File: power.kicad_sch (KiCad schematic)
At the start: 12 parts, among them J1 Conn_01x06_Pin, U3 LM66100DCK, U4 TPS62A01DRLR, U5 TPS22918TDBVRQ1

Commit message: Update power.kicad_sch
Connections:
- net +5V: no longer J1.3 (Pin_3)
- net GND: no longer J1.4 (Pin_4)
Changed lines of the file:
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@@
 	(wire
 		(pts
-			(xy 24.13 92.71) (xy 40.64 92.71)
+			(xy 24.13 92.71) (xy 36.83 92.71)
 		)
 		(stroke
@@
 	(wire
 		(pts
-			(xy 24.13 95.25) (xy 36.83 95.25)
+			(xy 148.59 64.77) (xy 160.02 64.77)
 		)
 		(stroke
@@
 	(wire
 		(pts
-			(xy 148.59 64.77) (xy 160.02 64.77)
+			(xy 148.59 74.93) (xy 160.02 74.93)
 		)
 		(stroke
@@
 	(wire
 		(pts
-			(xy 148.59 74.93) (xy 160.02 74.93)
+			(xy 172.72 72.39) (xy 176.53 72.39)
 		)
 		(stroke
@@
 	(wire
 		(pts
-			(xy 172.72 72.39) (xy 176.53 72.39)
+			(xy 172.72 64.77) (xy 180.34 64.77)
 		)
 		(stroke
@@
 	(wire
 		(pts
-			(xy 172.72 64.77) (xy 180.34 64.77)
+			(xy 160.02 64.77) (xy 172.72 64.77)
 		)
 		(stroke
@@
 	(wire
 		(pts
-			(xy 160.02 64.77) (xy 172.72 64.77)
+			(xy 160.02 64.77) (xy 160.02 66.04)
 		)
 		(stroke
@@
 	(wire
 		(pts
-			(xy 24.13 97.79) (xy 40.64 97.79)
+			(xy 44.45 69.85) (xy 44.45 82.55)
 		)
 		(stroke
@@
 	(wire
 		(pts
-			(xy 160.02 64.77) (xy 160.02 66.04)
+			(xy 67.31 82.55) (xy 67.31 64.77)
 		)
 		(stroke
@@
 	(wire
 		(pts
-			(xy 44.45 69.85) (xy 44.45 82.55)
-		)
-		(stroke
-			(width 0)
-			(type default)
-		)
-	)
-	(wire
-		(pts
-			(xy 67.31 82.55) (xy 67.31 64.77)
-		)
-		(stroke
-			(width 0)
-			(type default)
-		)
-	)
-	(wire
-		(pts
 			(xy 44.45 82.55) (xy 67.31 82.55)
-		)
-		(stroke
-			(width 0)
-			(type default)
-		)
-	)
-	(wire
-		(pts
-			(xy 36.83 102.87) (xy 40.64 102.87)
 		)
 		(stroke
@@
 	)
 	(symbol
-		(lib_id "power:GND")
-		(at 40.64 97.79 90)
-		(unit 1)
-		(exclude_from_sim no)
-		(in_bom yes)
-		(on_board yes)
-		(dnp no)
-		(fields_autoplaced yes)
-		(property "Reference" "#PWR033"
-			(at 46.99 97.79 0)
-			(effects
-				(font
-					(size 1.27 1.27)
-				)
-				(hide yes)
-			)
-		)
-		(property "Value" "GND"
-			(at 44.45 97.7899 90)
-			(effects
-				(font
-					(size 1.27 1.27)
-				)
-				(justify right)
-			)
-		)
-		(property "Footprint" ""
-			(at 40.64 97.79 0)
-			(effects
-				(font
-					(size 1.27 1.27)
-				)
-				(hide yes)
-			)
-		)
-		(property "Datasheet" ""
-			(at 40.64 97.79 0)
-			(effects
-				(font
-					(size 1.27 1.27)
-				)
-				(hide yes)
-			)
-		)
-		(property "Description" "Power symbol creates a global label with name \"GND\" , ground"
-			(at 40.64 97.79 0)
-			(effects
-				(font
-					(size 1.27 1.27)
-				)
-				(hide yes)
-			)
-		)
-		(pin "1"
-		)
-		(instances
-			(project ""
-				(path "/45f99759-2553-47c9-8640-9aec1810c6cc/7b2d3bba-bbf7-4c7f-a096-b989c0e14168"
-					(reference "#PWR033")
-					(unit 1)
-				)
-			)
-		)
-	)
-	(symbol
 		(lib_id "Device:C")
 		(at 172.72 68.58 0)
@@
 	)
 	(symbol
-		(lib_id "power:+5V")
-		(at 36.83 95.25 270)
-		(unit 1)
-		(exclude_from_sim no)
-		(in_bom yes)
-		(on_board yes)
-		(dnp no)
-		(fields_autoplaced yes)
-		(property "Reference" "#PWR045"
-			(at 33.02 95.25 0)
-			(effects
-				(font
-					(size 1.27 1.27)
-				)
-				(hide yes)
-			)
-		)
-		(property "Value" "+5V"
-			(at 40.64 95.2499 90)
-			(effects
-				(font
-					(size 1.27 1.27)
-				)
-				(justify left)
-			)
-		)
-		(property "Footprint" ""
-			(at 36.83 95.25 0)
-			(effects
-				(font
-					(size 1.27 1.27)
-				)
-				(hide yes)
-			)
-		)
-		(property "Datasheet" ""
-			(at 36.83 95.25 0)
-			(effects
-				(font
-					(size 1.27 1.27)
-				)
-				(hide yes)
-			)
-		)
-		(property "Description" "Power symbol creates a global label with name \"+5V\""
-			(at 36.83 95.25 0)
-			(effects
-				(font
-					(size 1.27 1.27)
-				)
-				(hide yes)
-			)
-		)
-		(pin "1"
-		)
-		(instances
-			(project ""
-				(path "/45f99759-2553-47c9-8640-9aec1810c6cc/7b2d3bba-bbf7-4c7f-a096-b989c0e14168"
-					(reference "#PWR045")
-					(unit 1)
-				)
-			)
-		)
-	)
-	(symbol
 		(lib_id "Device:C")
 		(at 107.95 83.82 0)
@@
 	(symbol
 		(lib_id "power:GND")
-		(at 40.64 92.71 90)
+		(at 36.83 92.71 90)
 		(unit 1)
 		(exclude_from_sim no)
@@
 		(fields_autoplaced yes)
 		(property "Reference" "#PWR032"
-			(at 46.99 92.71 0)
+			(at 43.18 92.71 0)
 			(effects
 				(font
@@
 		)
 		(property "Value" "GND"
-			(at 44.45 92.7099 90)
+			(at 40.64 92.7099 90)
 			(effects
 				(font
@@
 		)
 		(property "Footprint" ""
-			(at 40.64 92.71 0)
+			(at 36.83 92.71 0)
 			(effects
 				(font
@@
 		)
 		(property "Datasheet" ""
-			(at 40.64 92.71 0)
+			(at 36.83 92.71 0)
 			(effects
 				(font
@@
 		)
 		(property "Description" "Power symbol creates a global label with name \"GND\" , ground"
-			(at 40.64 92.71 0)
+			(at 36.83 92.71 0)
 			(effects
 				(font
@@
 	(symbol
 		(lib_id "power:GND")
-		(at 40.64 102.87 90)
+		(at 36.83 102.87 90)
 		(unit 1)
 		(exclude_from_sim no)
@@
 		(fields_autoplaced yes)
 		(property "Reference" "#PWR034"
-			(at 46.99 102.87 0)
+			(at 43.18 102.87 0)
 			(effects
 				(font
@@
 		)
 		(property "Value" "GND"
-			(at 44.45 102.8699 90)
+			(at 40.64 102.8699 90)
 			(effects
 				(font
@@
 		)
 		(property "Footprint" ""
-			(at 40.64 102.87 0)
+			(at 36.83 102.87 0)
 			(effects
 				(font
@@
 		)
 		(property "Datasheet" ""
-			(at 40.64 102.87 0)
+			(at 36.83 102.87 0)
 			(effects
 				(font
@@
 		)
 		(property "Description" "Power symbol creates a global label with name \"GND\" , ground"
-			(at 40.64 102.87 0)
-			(effects
-				(font
+			(at 36.83 102.87 0)
+			(effects
+				(font

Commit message: Ripple Filter
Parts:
- removed U4: TPS62A01DRLR, SOT6_DRL_TEX, symbol TPS62A01:TPS62A01DRLR
- added C11: 10uF, symbol Device:C
- added C12: 22uF, symbol Device:C
- added L5: 10uH, symbol Device:L
- added R11: 1, symbol Device:R_US
- C6: value 1nF -> 330pF
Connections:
- net 5V_SW: now also L5.1
- net GND: now also C11.1, C12.2
- new net: C12.1, R11.2
- new net 5V_F: C11.2, L5.2, R11.1
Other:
- added sheet D_Filter_Sim (untitled.kicad_sch)
- moved on the sheet: C6

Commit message: Ripple Filter
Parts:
- removed C4: 100n, symbol Device:C
- added R12: 100k, symbol Device:R_US
- R7: value 1k -> 10k
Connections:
- net GND: now also R12.2; no longer R7.2
- net RF_PWR_EN: now also R7.1; no longer U5.3 (ON)
- net at C5.1, U3.3 (~{CE}), U3.6 (VOUT)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: no longer R7.1
- new net: R12.1, R7.2, U5.3 (ON)
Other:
- removed sheet D_Filter_Sim
- note added: "LC low-pass for PWR-2/4 ripple"
- moved on the sheet: C5, R8

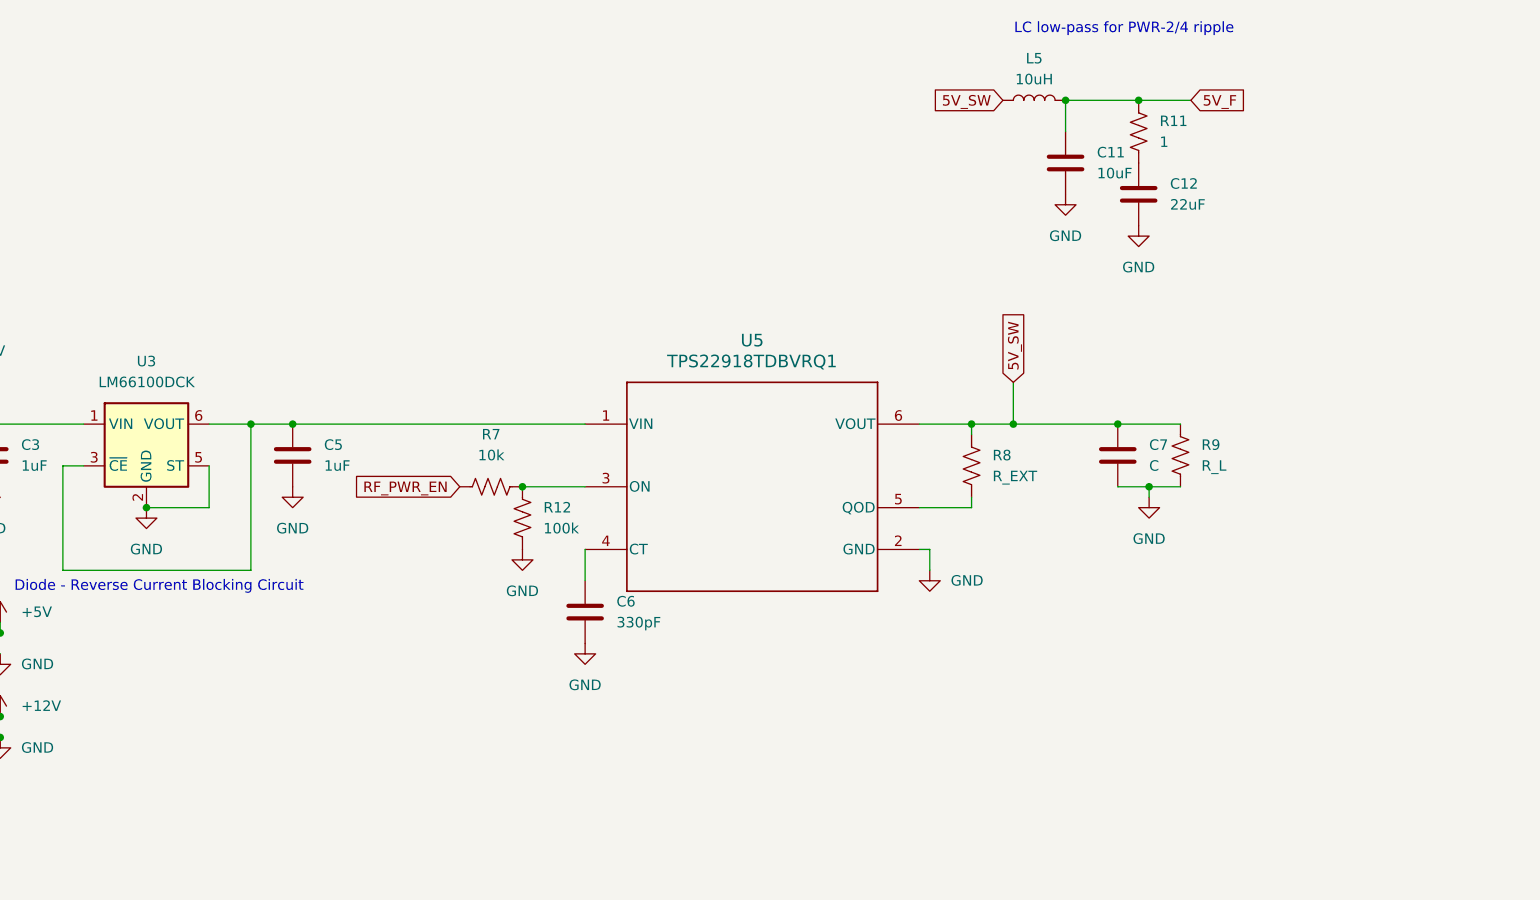
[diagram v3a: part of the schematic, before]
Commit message: Placing both LDOs
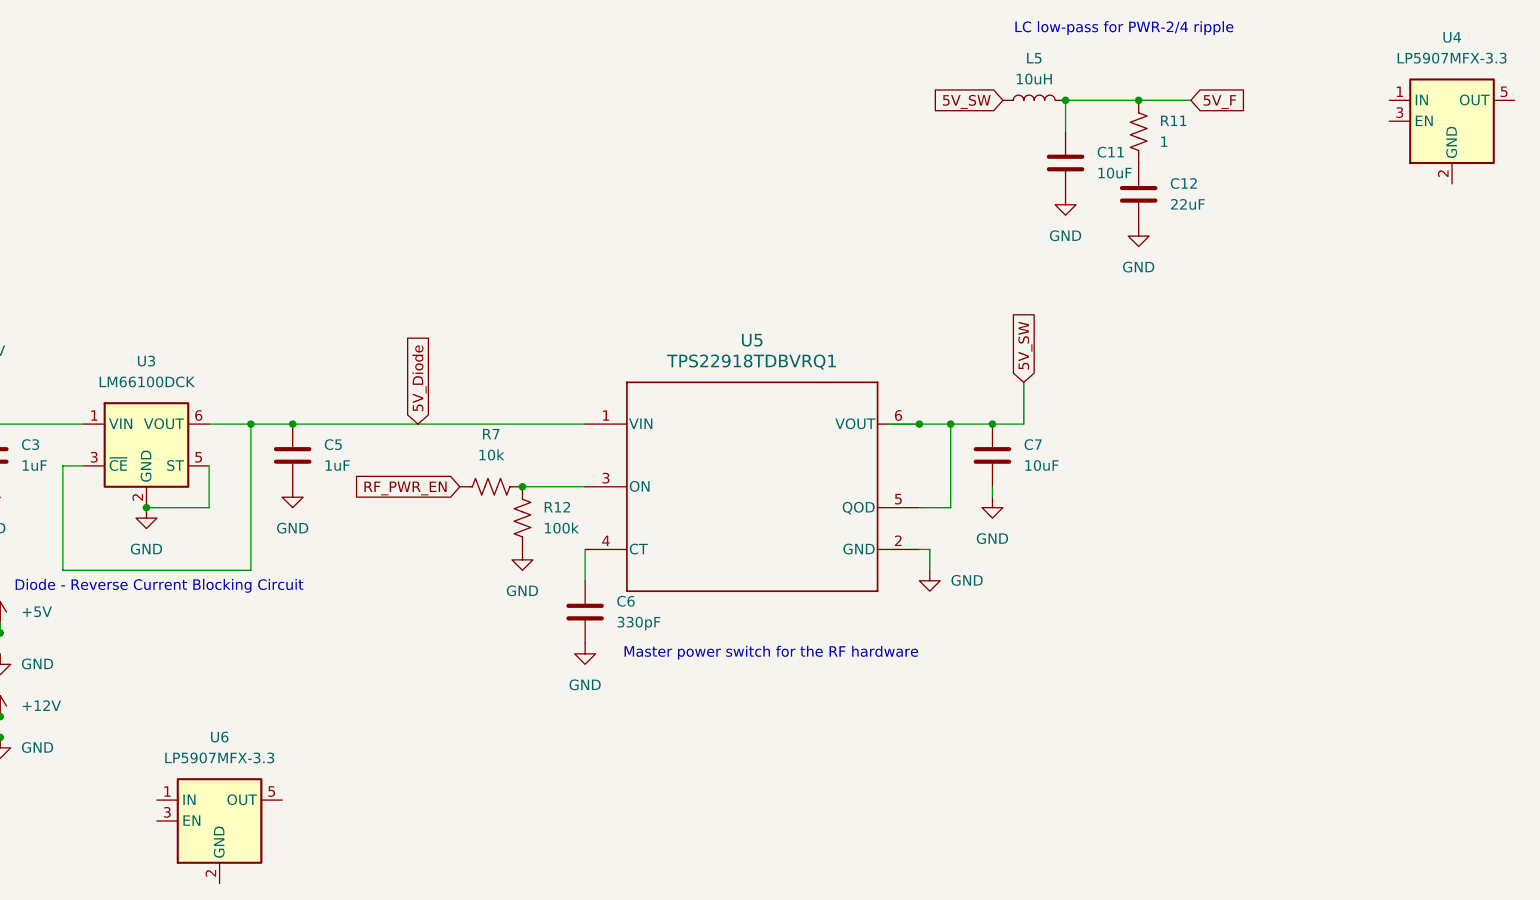
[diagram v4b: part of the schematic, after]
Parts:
- removed R8: R_EXT, symbol Device:R_US
- removed R9: R_L, symbol Device:R_US
- added U4, U6: LP5907MFX-3.3, Package_TO_SOT_SMD:SOT-23-5, symbol Regulator_Linear:LP5907MFX-3.3
- C7: value C -> 10uF
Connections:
- net 5V_SW: now also U5.5 (QOD)
- net 5V_Diode: now reaches C5.1, U3.3 (~{CE}), U3.6 (VOUT), U5.1 (VIN)
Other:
- note added: "Master power switch for the RF hardware"
- moved on the sheet: C7

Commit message: LDO
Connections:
- net 5V_F: now also U4.1 (IN)
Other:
- moved on the sheet: U4
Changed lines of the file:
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@@
+		)
+	)
+	(global_label "5V_F"
+		(shape input)
+		(at 213.36 41.91 180)
+		(fields_autoplaced yes)
+		(effects
+			(font
+				(size 1.27 1.27)
+			)
+			(justify right)
+		)
+		(property "Intersheetrefs" "${INTERSHEET_REFS}"
+			(at 206.0205 41.91 0)
+			(effects
+				(font
+					(size 1.27 1.27)
+				)
+				(justify right)
+				(hide yes)
+			)
 		)
 	)
@@
 	(symbol
 		(lib_id "Regulator_Linear:LP5907MFX-3.3")
-		(at 213.36 27.94 0)
+		(at 220.98 44.45 0)
 		(unit 1)
 		(exclude_from_sim no)
@@
 		(fields_autoplaced yes)
 		(property "Reference" "U4"
-			(at 213.36 17.78 0)
+			(at 220.98 34.29 0)
 			(effects
 				(font
@@
 		)
 		(property "Value" "LP5907MFX-3.3"
-			(at 213.36 20.32 0)
+			(at 220.98 36.83 0)
 			(effects
 				(font
@@
 		)
 		(property "Footprint" "Package_TO_SOT_SMD:SOT-23-5"
-			(at 213.36 19.05 0)
+			(at 220.98 35.56 0)
 			(effects
 				(font
@@
 		)
 		(property "Datasheet" "http://www.ti.com/lit/ds/symlink/lp5907.pdf"
-			(at 213.36 15.24 0)
+			(at 220.98 31.75 0)
 			(effects
 				(font
@@
 		)
 		(property "Description" "250-mA Ultra-Low-Noise Low-IQ LDO, 3.3V, SOT-23"
-			(at 213.36 27.94 0)
-			(effects
-				(font
+			(at 220.98 44.45 0)
+			(effects
+				(font

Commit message: LDOs
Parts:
- removed U4, U6: LP5907MFX-3.3, Package_TO_SOT_SMD:SOT-23-5, symbol Regulator_Linear:LP5907MFX-3.3
- added U13, U4, U6: LP5907MFX-3.0, Package_TO_SOT_SMD:SOT-23-5, symbol Regulator_Linear:LP5907MFX-3.0
- added U14: LP5907MFX-4.5, Package_TO_SOT_SMD:SOT-23-5, symbol Regulator_Linear:LP5907MFX-4.5
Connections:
- net 5V_F: now also U13.1 (IN)
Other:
- note added: "LDO for RF"
- note added: "LDO for Telemetry"
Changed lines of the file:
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@@
+	)
+	(junction
+		(at 87.63 64.77)
+		(diameter 0)
+		(color 0 0 0 0)
 	)
 	(junction
@@
 	(wire
 		(pts
+			(xy 87.63 62.23) (xy 87.63 64.77)
+		)
+		(stroke
+			(width 0)
+			(type default)
+		)
+	)
+	(wire
+		(pts
 			(xy 166.37 25.4) (xy 175.26 25.4)
 		)
@@
 	(wire
 		(pts
+			(xy 87.63 64.77) (xy 107.95 64.77)
+		)
+		(stroke
+			(width 0)
+			(type default)
+		)
+	)
+	(wire
+		(pts
 			(xy 62.23 69.85) (xy 62.23 74.93)
 		)
@@
 	(wire
 		(pts
-			(xy 72.39 64.77) (xy 107.95 64.77)
+			(xy 72.39 64.77) (xy 87.63 64.77)
 		)
 		(stroke
@@
 		)
 	)
+	(text "LDO for Telemetry"
+		(exclude_from_sim no)
+		(at 62.484 118.11 0)
+		(effects
+			(font
+				(size 1.27 1.27)
+			)
+		)
+	)
 	(text "Master power switch for the RF hardware"
 		(exclude_from_sim no)
@@
 		)
 	)
+	(text "LDO for RF"
+		(exclude_from_sim no)
+		(at 221.234 55.372 0)
+		(effects
+			(font
+				(size 1.27 1.27)
+			)
+		)
+	)
 	(global_label "5V_F"
 		(shape input)
@@
 	(global_label "5V_Diode"
 		(shape input)
-		(at 87.63 64.77 90)
+		(at 87.63 62.23 90)
 		(fields_autoplaced yes)
 		(effects
@@
 		)
 		(property "Intersheetrefs" "${INTERSHEET_REFS}"
-			(at 87.63 53.2577 90)
+			(at 87.63 50.7177 90)
 			(effects
 				(font
@@
 	)
 	(symbol
+		(lib_id "Regulator_Linear:LP5907MFX-3.0")
+		(at 38.1 149.86 0)
+		(unit 1)
+		(exclude_from_sim no)
+		(in_bom yes)
+		(on_board yes)
+		(dnp no)
+		(fields_autoplaced yes)
+		(property "Reference" "U6"
+			(at 38.1 139.7 0)
+			(effects
+				(font
+					(size 1.27 1.27)
+				)
+			)
+		)
+		(property "Value" "LP5907MFX-3.0"
+			(at 38.1 142.24 0)
+			(effects
+				(font
+					(size 1.27 1.27)
+				)
+			)
+		)
+		(property "Footprint" "Package_TO_SOT_SMD:SOT-23-5"
+			(at 38.1 140.97 0)
+			(effects
+				(font
+					(size 1.27 1.27)
+				)
+				(hide yes)
+			)
+		)
+		(property "Datasheet" "http://www.ti.com/lit/ds/symlink/lp5907.pdf"
+			(at 38.1 137.16 0)
+			(effects
+				(font
+					(size 1.27 1.27)
+				)
+				(hide yes)
+			)
+		)
+		(property "Description" "250-mA Ultra-Low-Noise Low-IQ LDO, 3.0V, SOT-23"
+			(at 38.1 149.86 0)
+			(effects
+				(font
+					(size 1.27 1.27)
+				)
+				(hide yes)
+			)
+		)
+		(pin "3"
+		)
+		(pin "1"
+		)
+		(pin "2"
+		)
+		(pin "4"
+		)
+		(pin "5"
+		)
+		(instances
+			(project "VIP_direct_sampling_board"
+				(path "/45f99759-2553-47c9-8640-9aec1810c6cc/7b2d3bba-bbf7-4c7f-a096-b989c0e14168"
+					(reference "U6")
+					(unit 1)
+				)
+			)
+		)
+	)
+	(symbol
+		(lib_id "Regulator_Linear:LP5907MFX-3.0")
+		(at 220.98 44.45 0)
+		(unit 1)
+		(exclude_from_sim no)
+		(in_bom yes)
+		(on_board yes)
+		(dnp no)
+		(fields_autoplaced yes)
+		(property "Reference" "U13"
+			(at 220.98 34.29 0)
+			(effects
+				(font
+					(size 1.27 1.27)
+				)
+			)
+		)
+		(property "Value" "LP5907MFX-3.0"
+			(at 220.98 36.83 0)
+			(effects
+				(font
+					(size 1.27 1.27)
+				)
+			)
+		)
+		(property "Footprint" "Package_TO_SOT_SMD:SOT-23-5"
+			(at 220.98 35.56 0)
+			(effects
+				(font
+					(size 1.27 1.27)
+				)
+				(hide yes)
+			)
+		)
+		(property "Datasheet" "http://www.ti.com/lit/ds/symlink/lp5907.pdf"
+			(at 220.98 31.75 0)
+			(effects
+				(font
+					(size 1.27 1.27)
+				)
+				(hide yes)
+			)
+		)
+		(property "Description" "250-mA Ultra-Low-Noise Low-IQ LDO, 3.0V, SOT-23"
+			(at 220.98 44.45 0)
+			(effects
+				(font
+					(size 1.27 1.27)
+				)
+				(hide yes)
+			)
+		)
+		(pin "3"
+		)
+		(pin "1"
+		)
+		(pin "2"
+		)
+		(pin "4"
+		)
+		(pin "5"
+		)
+		(instances
+			(project ""
+				(path "/45f99759-2553-47c9-8640-9aec1810c6cc/7b2d3bba-bbf7-4c7f-a096-b989c0e14168"
+					(reference "U13")
+					(unit 1)
+				)
+			)
+		)
+	)
+	(symbol
 		(lib_id "Device:C")
 		(at 157.48 68.58 0)
@@
 	)
 	(symbol
-		(lib_id "Regulator_Linear:LP5907MFX-3.3")
-		(at 63.5 113.03 0)
-		(unit 1)
-		(exclude_from_sim no)
-		(in_bom yes)
-		(on_board yes)
-		(dnp no)
-		(fields_autoplaced yes)
-		(property "Reference" "U6"
-			(at 63.5 102.87 0)
-			(effects
-				(font
-					(size 1.27 1.27)
-				)
-			)
-		)
-		(property "Value" "LP5907MFX-3.3"
-			(at 63.5 105.41 0)
+		(lib_id "Regulator_Linear:LP5907MFX-4.5")
+		(at 101.6 151.13 0)
+		(unit 1)
+		(exclude_from_sim no)
+		(in_bom yes)
+		(on_board yes)
+		(dnp no)
+		(fields_autoplaced yes)
+		(property "Reference" "U14"
+			(at 101.6 140.97 0)
+			(effects
+				(font
+					(size 1.27 1.27)
+				)
+			)
+		)
+		(property "Value" "LP5907MFX-4.5"
+			(at 101.6 143.51 0)
 			(effects
 				(font
@@
 		)
 		(property "Footprint" "Package_TO_SOT_SMD:SOT-23-5"
-			(at 63.5 104.14 0)
+			(at 101.6 142.24 0)
 			(effects
 				(font
@@
 		)
 		(property "Datasheet" "http://www.ti.com/lit/ds/symlink/lp5907.pdf"
-			(at 63.5 100.33 0)
-			(effects
-				(font
-					(size 1.27 1.27)
-				)
-				(hide yes)
-			)
-		)
-		(property "Description" "250-mA Ultra-Low-Noise Low-IQ LDO, 3.3V, SOT-23"
-			(at 63.5 113.03 0)
-			(effects
-				(font
-					(size 1.27 1.27)
-				)
-				(hide yes)
-			)
-		)
-		(pin "1"
+			(at 101.6 138.43 0)
+			(effects
+				(font
+					(size 1.27 1.27)
+				)
+				(hide yes)
+			)
+		)
+		(property "Description" "250-mA Ultra-Low-Noise Low-IQ LDO, 4.5V, SOT-23"
+			(at 101.6 151.13 0)
+			(effects
+				(font
+					(size 1.27 1.27)
+				)
+				(hide yes)
+			)
 		)
 		(pin "2"
 		)
+		(pin "1"
+		)
 		(pin "3"
 		)
@@
 		)
 		(instances
-			(project "VIP_direct_sampling_board"
-				(path "/45f99759-2553-47c9-8640-9aec1810c6cc/7b2d3bba-bbf7-4c7f-a096-b989c0e14168"
-					(reference "U6")
+			(project ""
+				(path "/45f99759-2553-47c9-8640-9aec1810c6cc/7b2d3bba-bbf7-4c7f-a096-b989c0e14168"
+					(reference "U14")
 					(unit 1)
 				)
@@
 	)
 	(symbol
-		(lib_id "Regulator_Linear:LP5907MFX-3.3")
-		(at 220.98 44.45 0)
+		(lib_id "Regulator_Linear:LP5907MFX-3.0")
+		(at 62.23 106.68 0)
 		(unit 1)
 		(exclude_from_sim no)
@@
 		(fields_autoplaced yes)
 		(property "Reference" "U4"
-			(at 220.98 34.29 0)
-			(effects
-				(font
-					(size 1.27 1.27)
-				)
-			)
-		)
-		(property "Value" "LP5907MFX-3.3"
-			(at 220.98 36.83 0)
+			(at 62.23 96.52 0)
+			(effects
+				(font
+					(size 1.27 1.27)
+				)
+			)
+		)
+		(property "Value" "LP5907MFX-3.0"
+			(at 62.23 99.06 0)
 			(effects
 				(font
@@
 		)
 		(property "Footprint" "Package_TO_SOT_SMD:SOT-23-5"
-			(at 220.98 35.56 0)
+			(at 62.23 97.79 0)
 			(effects
 				(font
@@
 		)
 		(property "Datasheet" "http://www.ti.com/lit/ds/symlink/lp5907.pdf"
-			(at 220.98 31.75 0)
-			(effects
-				(font
-					(size 1.27 1.27)
-				)
-				(hide yes)
-			)
-		)
-		(property "Description" "250-mA Ultra-Low-Noise Low-IQ LDO, 3.3V, SOT-23"
-			(at 220.98 44.45 0)
-			(effects
-				(font
-					(size 1.27 1.27)
-				)
-				(hide yes)
-			)
+			(at 62.23 93.98 0)
+			(effects
+				(font
+					(size 1.27 1.27)
+				)
+				(hide yes)
+			)
+		)
+		(property "Description" "250-mA Ultra-Low-Noise Low-IQ LDO, 3.0V, SOT-23"
+			(at 62.23 106.68 0)
+			(effects
+				(font
+					(size 1.27 1.27)
+				)
+				(hide yes)
+			)
+		)
+		(pin "3"
 		)
 		(pin "1"
@@
 		(pin "2"
 		)
-		(pin "3"
-		)
 		(pin "4"
 		)
@@
 		)
 		(instances
-			(project ""
+			(project "VIP_direct_sampling_board"
 				(path "/45f99759-2553-47c9-8640-9aec1810c6cc/7b2d3bba-bbf7-4c7f-a096-b989c0e14168"
 					(reference "U4")
